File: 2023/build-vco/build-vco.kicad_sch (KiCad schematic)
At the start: 7 parts, among them M1 PMOS_OR1, M2 NMOS_OR1, M27 NMOS_OR1, M3 PMOS_OR1, M4 NMOS_OR1, M5 NMOS_OR1, M7 NMOS_OR1

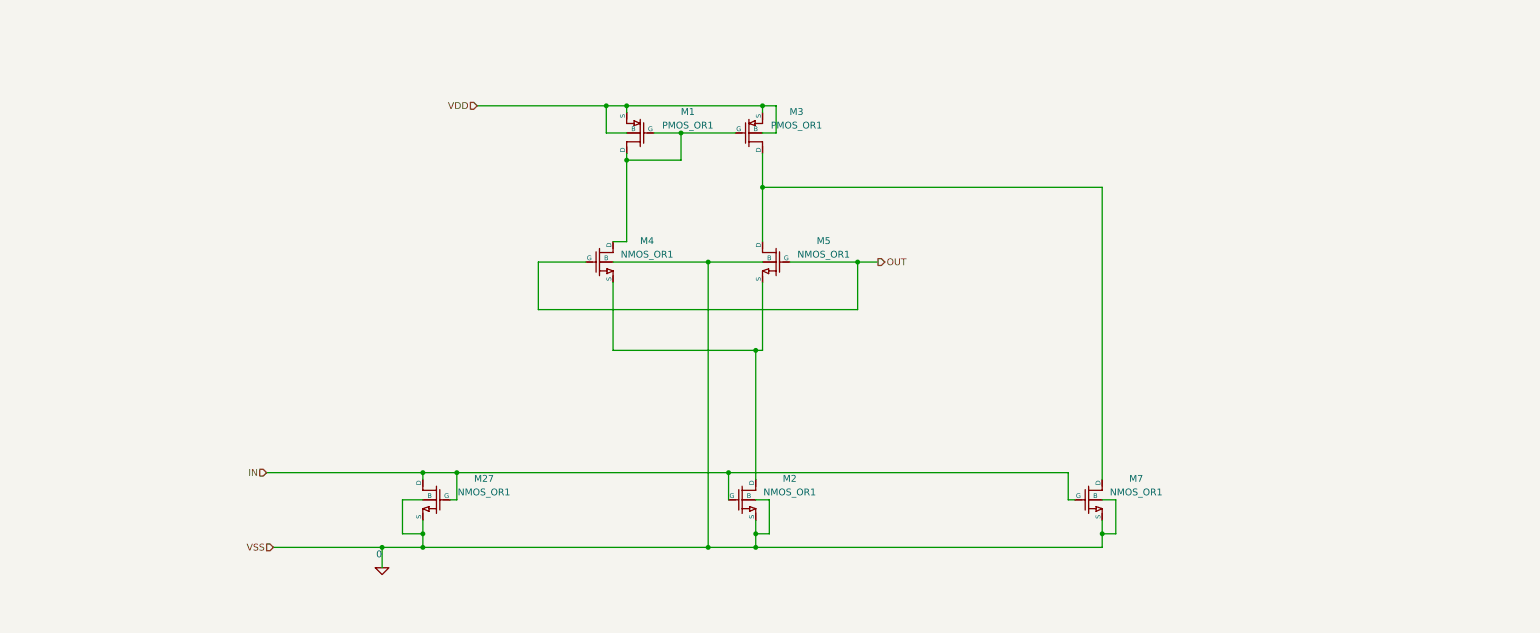
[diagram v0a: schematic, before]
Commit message: 2段で Out2 を増やした。2段で Out2 を増やした。
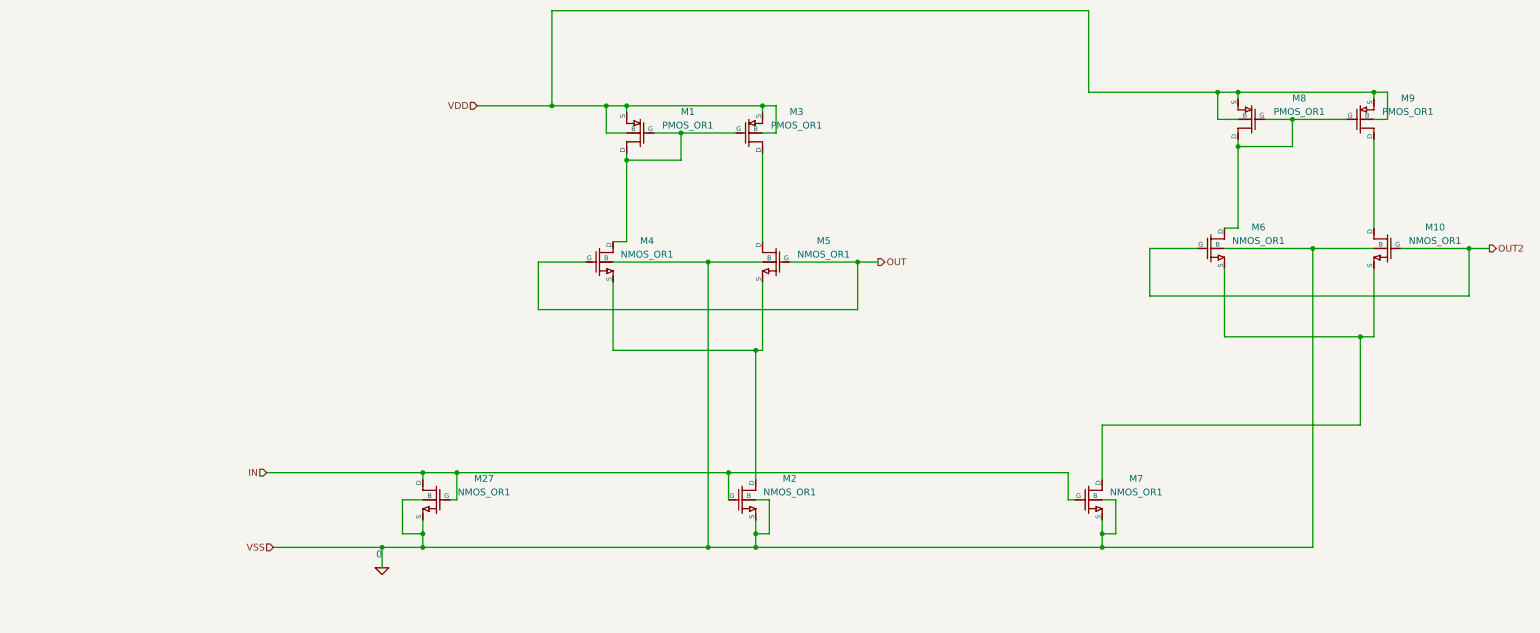
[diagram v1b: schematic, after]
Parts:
- added M10, M6: NMOS_OR1, symbol OR1Symbols:NMOS_OR1
- added M8, M9: PMOS_OR1, symbol OR1Symbols:PMOS_OR1
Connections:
- net 0: now also M10.4 (B), M6.4 (B)
- net VDD: now also M8.3 (S), M8.4 (B), M9.3 (S), M9.4 (B)
- net at M3.1 (D), M5.1 (D): no longer M7.1 (D)
- new net: M6.1 (D), M8.1 (D), M8.2 (G), M9.2 (G)
- new net: M10.3 (S), M6.3 (S), M7.1 (D)
- new net: M10.1 (D), M9.1 (D)
- new net OUT2: M10.2 (G), M6.2 (G)

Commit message: OUT2 を削除し、次の段につなげる。LVS OK.
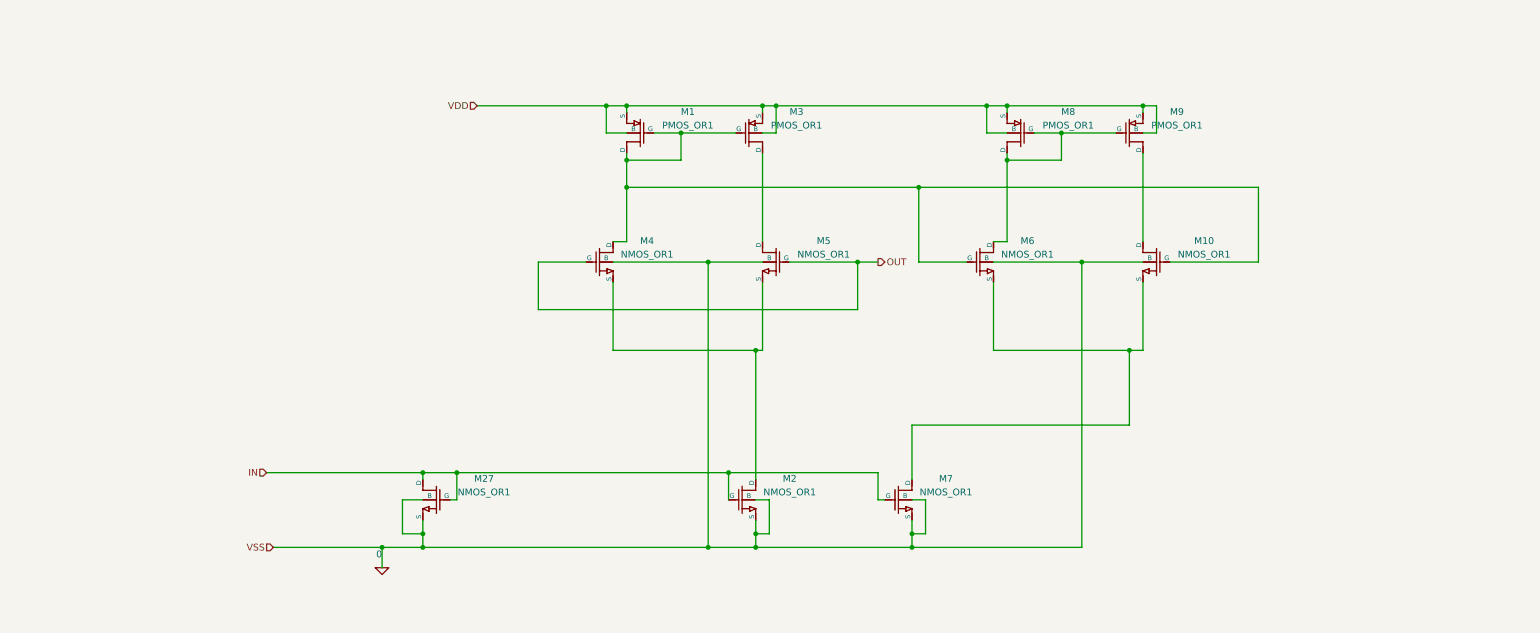
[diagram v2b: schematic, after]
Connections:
- net OUT2 is gone; now on an unnamed net: M10.2 (G), M6.2 (G)
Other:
- moved on the sheet: M10, M6, M7, M8, M9

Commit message: 二段にして LVS OK.
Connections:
- net at M1.1 (D), M1.2 (G), M3.2 (G)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: no longer M10.2 (G)
- net at M3.1 (D), M5.1 (D): now also M10.2 (G)

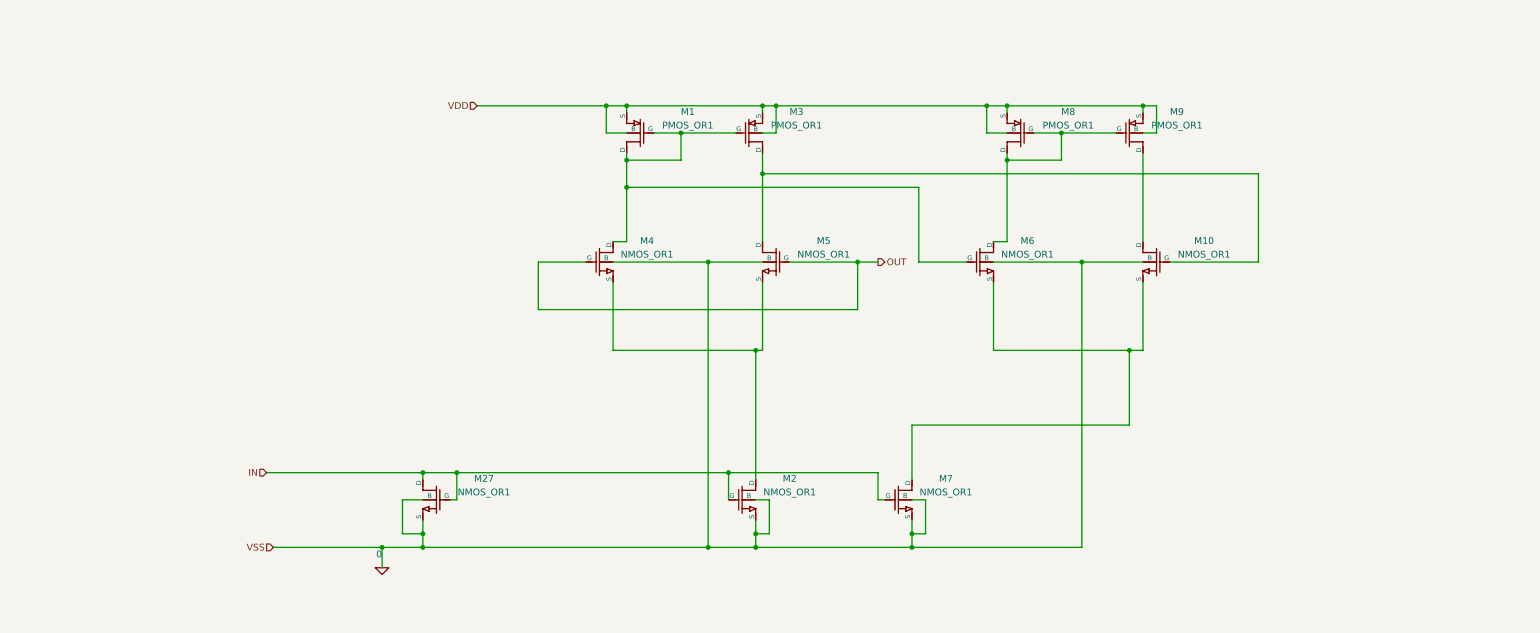
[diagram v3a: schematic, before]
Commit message: NMOS 増やして LVS OK.
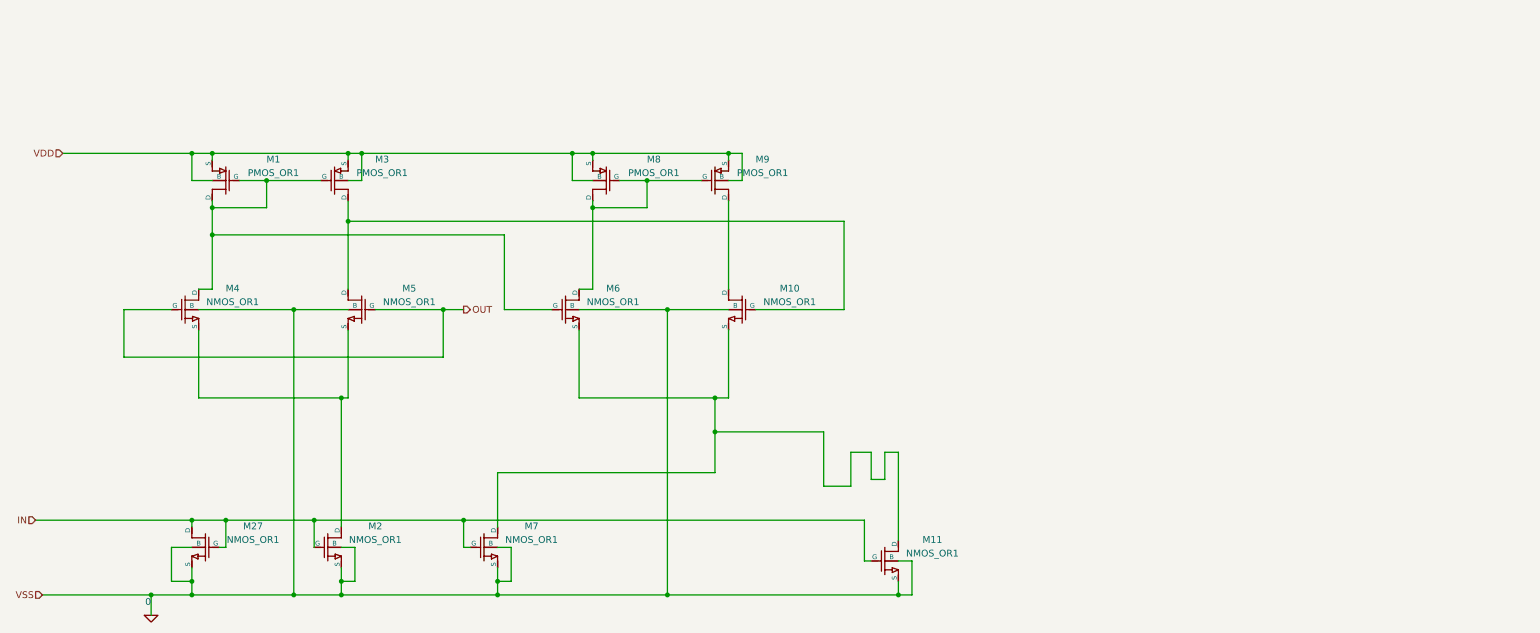
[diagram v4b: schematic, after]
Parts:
- added M11: NMOS_OR1, symbol OR1Symbols:NMOS_OR1
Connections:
- net 0: now also M11.3 (S), M11.4 (B)
- net IN: now also M11.2 (G)
- net at M10.3 (S), M6.3 (S), M7.1 (D): now also M11.1 (D)
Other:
- moved on the sheet: M1, M10, M2, M27, M3, M4, M5, M6, M7, M8, M9

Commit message: FB 追加。In と Out を IN と OUT に変更。LVS OK.
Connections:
- net OUT: no longer M4.2 (G)
- new net FB: M4.2 (G)
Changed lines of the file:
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@@
   (junction (at 78.74 143.51) (diameter 0) (color 0 0 0 0)
   )
-  (junction (at 97.79 92.71) (diameter 0) (color 0 0 0 0)
-  )
   (junction (at 125.73 63.5) (diameter 0) (color 0 0 0 0)
   )
@@
     (stroke (width 0) (type default))
   )
-  (wire (pts (xy 38.1 101.6) (xy 38.1 92.71))
-    (stroke (width 0) (type default))
-  )
   (wire (pts (xy 182.88 146.05) (xy 185.42 146.05))
     (stroke (width 0) (type default))
@@
     (stroke (width 0) (type default))
   )
-  (wire (pts (xy 97.79 92.71) (xy 101.6 92.71))
+  (wire (pts (xy 85.09 92.71) (xy 101.6 92.71))
     (stroke (width 0) (type default))
   )
@@
     (stroke (width 0) (type default))
   )
-  (wire (pts (xy 85.09 92.71) (xy 97.79 92.71))
-    (stroke (width 0) (type default))
-  )
   (wire (pts (xy 78.74 109.22) (xy 78.74 133.35))
     (stroke (width 0) (type default))
@@
     (stroke (width 0) (type default))
   )
-  (wire (pts (xy 97.79 92.71) (xy 97.79 101.6))
-    (stroke (width 0) (type default))
-  )
   (wire (pts (xy 80.01 76.2) (xy 80.01 88.9))
     (stroke (width 0) (type default))
@@
   )
   (wire (pts (xy 59.69 68.58) (xy 64.77 68.58))
-    (stroke (width 0) (type default))
-  )
-  (wire (pts (xy 97.79 101.6) (xy 38.1 101.6))
     (stroke (width 0) (type default))
   )
@@
     (effects (font (size 1.27 1.27)) (justify right))
   )
+  (hierarchical_label "FB" (shape input) (at 38.1 92.71 180) (fields_autoplaced)
+    (effects (font (size 1.27 1.27)) (justify right))
+  )
